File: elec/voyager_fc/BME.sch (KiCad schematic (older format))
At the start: 3 parts

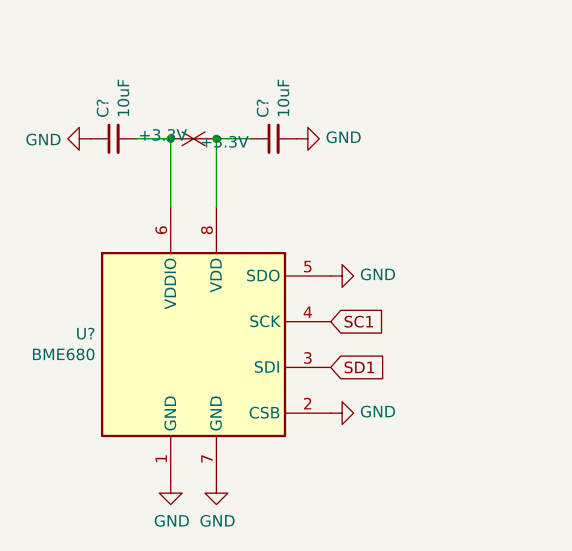
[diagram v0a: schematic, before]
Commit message: Place all components and start route
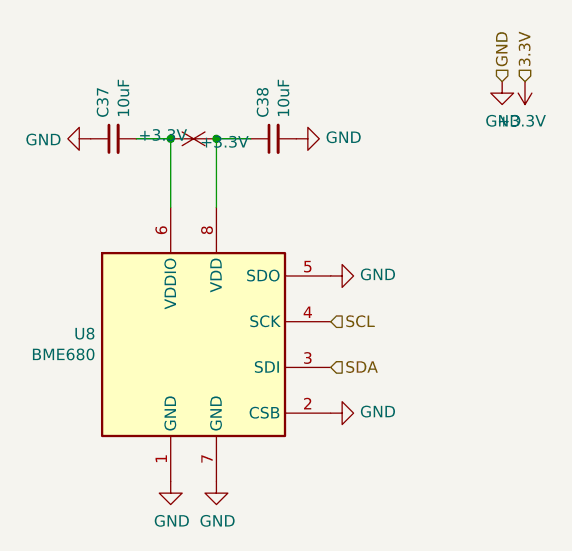
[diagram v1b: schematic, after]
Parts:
- C37, C38: renamed from C?; footprint Capacitor_SMD:C_0805_2012Metric -> Capacitor_SMD:C_0603_1608Metric
- gave numbers to parts that had none: 1
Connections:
- net SC1 renamed SCL
- net SD1 renamed SDA
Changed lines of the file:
@@
 $Descr A4 11693 8268
 encoding utf-8
-Sheet 8 9
+Sheet 7 10
 Title ""
 Date ""
@@
 U 1 1 67979F95
 P 5750 4550
-F 0 "#PWR?" H 5750 4300 50  0001 C CNN
+AR Path="/67979F95" Ref="#PWR?"  Part="1"
+AR Path="/67978800/67979F95" Ref="#PWR0164"  Part="1"
+F 0 "#PWR0164" H 5750 4300 50  0001 C CNN
 F 1 "GND" V 5755 4422 50  0000 R CNN
 F 2 "" H 5750 4550 50  0001 C CNN
@@
 U 1 1 67979F9B
 P 5750 3950
-F 0 "#PWR?" H 5750 3700 50  0001 C CNN
+AR Path="/67979F9B" Ref="#PWR?"  Part="1"
+AR Path="/67978800/67979F9B" Ref="#PWR0163"  Part="1"
+F 0 "#PWR0163" H 5750 3700 50  0001 C CNN
 F 1 "GND" V 5755 3822 50  0000 R CNN
 F 2 "" H 5750 3950 50  0001 C CNN
@@
 U 1 1 67979FA1
 P 5600 3350
-F 0 "#PWR?" H 5600 3100 50  0001 C CNN
+AR Path="/67979FA1" Ref="#PWR?"  Part="1"
+AR Path="/67978800/67979FA1" Ref="#PWR0162"  Part="1"
+F 0 "#PWR0162" H 5600 3100 50  0001 C CNN
 F 1 "GND" V 5605 3222 50  0000 R CNN
 F 2 "" H 5600 3350 50  0001 C CNN
@@
 U 1 1 67979FA7
 P 4700 3350
-F 0 "#PWR?" H 4700 3100 50  0001 C CNN
+AR Path="/67979FA7" Ref="#PWR?"  Part="1"
+AR Path="/67978800/67979FA7" Ref="#PWR0157"  Part="1"
+F 0 "#PWR0157" H 4700 3100 50  0001 C CNN
 F 1 "GND" V 4705 3222 50  0000 R CNN
 F 2 "" H 4700 3350 50  0001 C CNN
@@
 U 1 1 67979FAD
 P 5250 4850
-F 0 "#PWR?" H 5250 4600 50  0001 C CNN
+AR Path="/67979FAD" Ref="#PWR?"  Part="1"
+AR Path="/67978800/67979FAD" Ref="#PWR0161"  Part="1"
+F 0 "#PWR0161" H 5250 4600 50  0001 C CNN
 F 1 "GND" H 5255 4677 50  0000 C CNN
 F 2 "" H 5250 4850 50  0001 C CNN
@@
 U 1 1 67979FB3
 P 5050 4850
-F 0 "#PWR?" H 5050 4600 50  0001 C CNN
+AR Path="/67979FB3" Ref="#PWR?"  Part="1"
+AR Path="/67978800/67979FB3" Ref="#PWR0159"  Part="1"
+F 0 "#PWR0159" H 5050 4600 50  0001 C CNN
 F 1 "GND" H 5055 4677 50  0000 C CNN
 F 2 "" H 5050 4850 50  0001 C CNN
@@
 	1    0    0    -1
 $EndComp
-Text GLabel 5750 4350 2    50   Input ~ 0
-SD1
-Text GLabel 5750 4150 2    50   Input ~ 0
-SC1
 $Comp
 L Sensor:BME680 U?
 U 1 1 67979FBB
 P 5150 4250
-F 0 "U?" H 4721 4296 50  0000 R CNN
+AR Path="/67979FBB" Ref="U?"  Part="1"
+AR Path="/67978800/67979FBB" Ref="U8"  Part="1"
+F 0 "U8" H 4721 4296 50  0000 R CNN
 F 1 "BME680" H 4721 4205 50  0000 R CNN
 F 2 "Package_LGA:Bosch_LGA-8_3x3mm_P0.8mm_ClockwisePinNumbering" H 6600 3800 50  0001 C CNN
@@
 U 1 1 67979FC1
 P 4800 3350
-F 0 "C?" H 4892 3396 50  0000 L CNN
+AR Path="/67979FC1" Ref="C?"  Part="1"
+AR Path="/67978800/67979FC1" Ref="C37"  Part="1"
+F 0 "C37" H 4892 3396 50  0000 L CNN
 F 1 "10uF" H 4892 3305 50  0000 L CNN
-F 2 "Capacitor_SMD:C_0805_2012Metric" H 4800 3350 50  0001 C CNN
+F 2 "Capacitor_SMD:C_0603_1608Metric" H 4800 3350 50  0001 C CNN
 F 3 "~" H 4800 3350 50  0001 C CNN
 	1    4800 3350
@@
 U 1 1 67979FC7
 P 5500 3350
-F 0 "C?" H 5592 3396 50  0000 L CNN
+AR Path="/67979FC7" Ref="C?"  Part="1"
+AR Path="/67978800/67979FC7" Ref="C38"  Part="1"
+F 0 "C38" H 5592 3396 50  0000 L CNN
 F 1 "10uF" H 5592 3305 50  0000 L CNN
-F 2 "Capacitor_SMD:C_0805_2012Metric" H 5500 3350 50  0001 C CNN
+F 2 "Capacitor_SMD:C_0603_1608Metric" H 5500 3350 50  0001 C CNN
 F 3 "~" H 5500 3350 50  0001 C CNN
 	1    5500 3350
@@
 U 1 1 67979FCD
 P 5050 3350
-F 0 "#PWR?" H 5050 3200 50  0001 C CNN
+AR Path="/67979FCD" Ref="#PWR?"  Part="1"
+AR Path="/67978800/67979FCD" Ref="#PWR0158"  Part="1"
+F 0 "#PWR0158" H 5050 3200 50  0001 C CNN
 F 1 "+3.3V" V 5065 3478 50  0000 L CNN
 F 2 "" H 5050 3350 50  0001 C CNN
@@
 U 1 1 67979FD3
 P 5250 3350
-F 0 "#PWR?" H 5250 3200 50  0001 C CNN
+AR Path="/67979FD3" Ref="#PWR?"  Part="1"
+AR Path="/67978800/67979FD3" Ref="#PWR0160"  Part="1"
+F 0 "#PWR0160" H 5250 3200 50  0001 C CNN
 F 1 "+3.3V" V 5265 3478 50  0000 L CNN
 F 2 "" H 5250 3350 50  0001 C CNN
@@
 	5050 3350 5050 3650
 Connection ~ 5050 3350
+Text HLabel 5750 4150 2    50   Input ~ 0
+SCL
+Text HLabel 5750 4350 2    50   Input ~ 0
+SDA
+Text HLabel 6500 3100 1    50   Input ~ 0
+GND
+$Comp
+L power:GND #PWR0165
+U 1 1 67EF0901
+P 6500 3100
+F 0 "#PWR0165" H 6500 2850 50  0001 C CNN
+F 1 "GND" H 6505 2927 50  0000 C CNN
+F 2 "" H 6500 3100 50  0001 C CNN
+F 3 "" H 6500 3100 50  0001 C CNN
+	1    6500 3100
+	1    0    0    -1
+$EndComp
+$Comp
+L power:+3.3V #PWR0166
+U 1 1 67EF0DDA
+P 6600 3100
+F 0 "#PWR0166" H 6600 2950 50  0001 C CNN
+F 1 "+3.3V" H 6615 3273 50  0000 C CNN
+F 2 "" H 6600 3100 50  0001 C CNN
+F 3 "" H 6600 3100 50  0001 C CNN
+	1    6600 3100
+	-1   0    0    1
+$EndComp
+Text HLabel 6600 3100 1    50   Input ~ 0
+3.3V
 $EndSCHEMATC
